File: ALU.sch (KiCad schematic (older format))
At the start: 30 parts, among them U42 74LS245, U43 74LS00, U44 74LS86, U45 74LS86, U46 74LS86, U47 74LS00, U48 74LS86, U49 74HC02, U50 74LS00, U51 74LS00, U52 74LS283, U53 74LS85, U54 74LS283, U55 74LS245, U56 74LS85, U57 74LS245, U58 74LS283, U59 74LS85, U60 74LS173, U61 74LS283, U62 74LS245, U63 74LS85

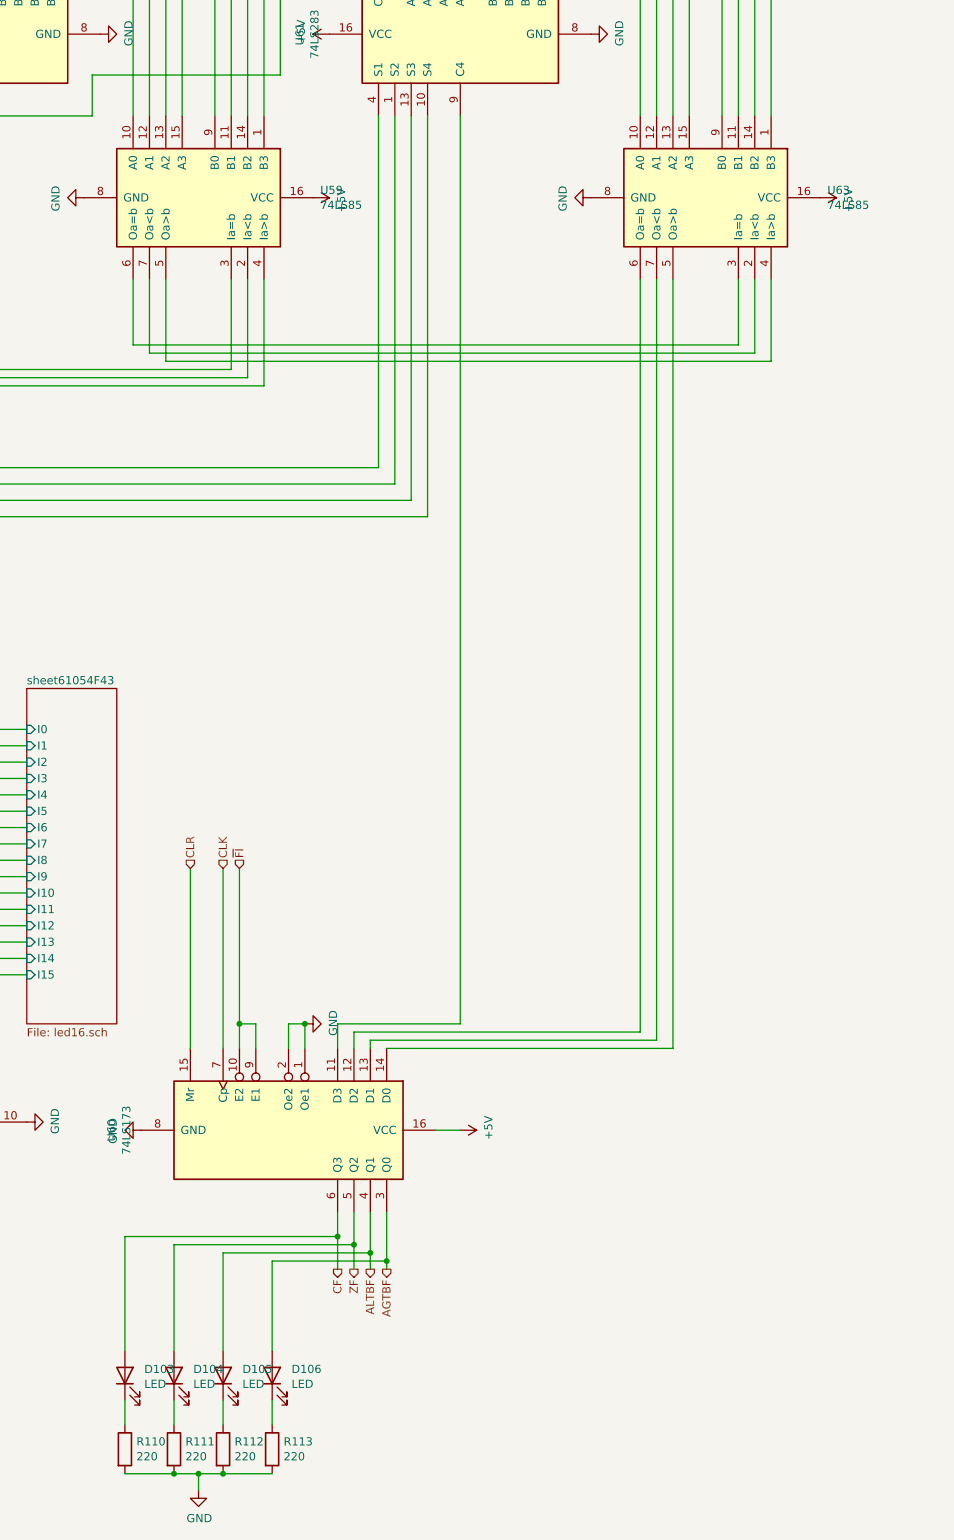
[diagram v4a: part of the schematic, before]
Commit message: added 3-8 decoders to cu
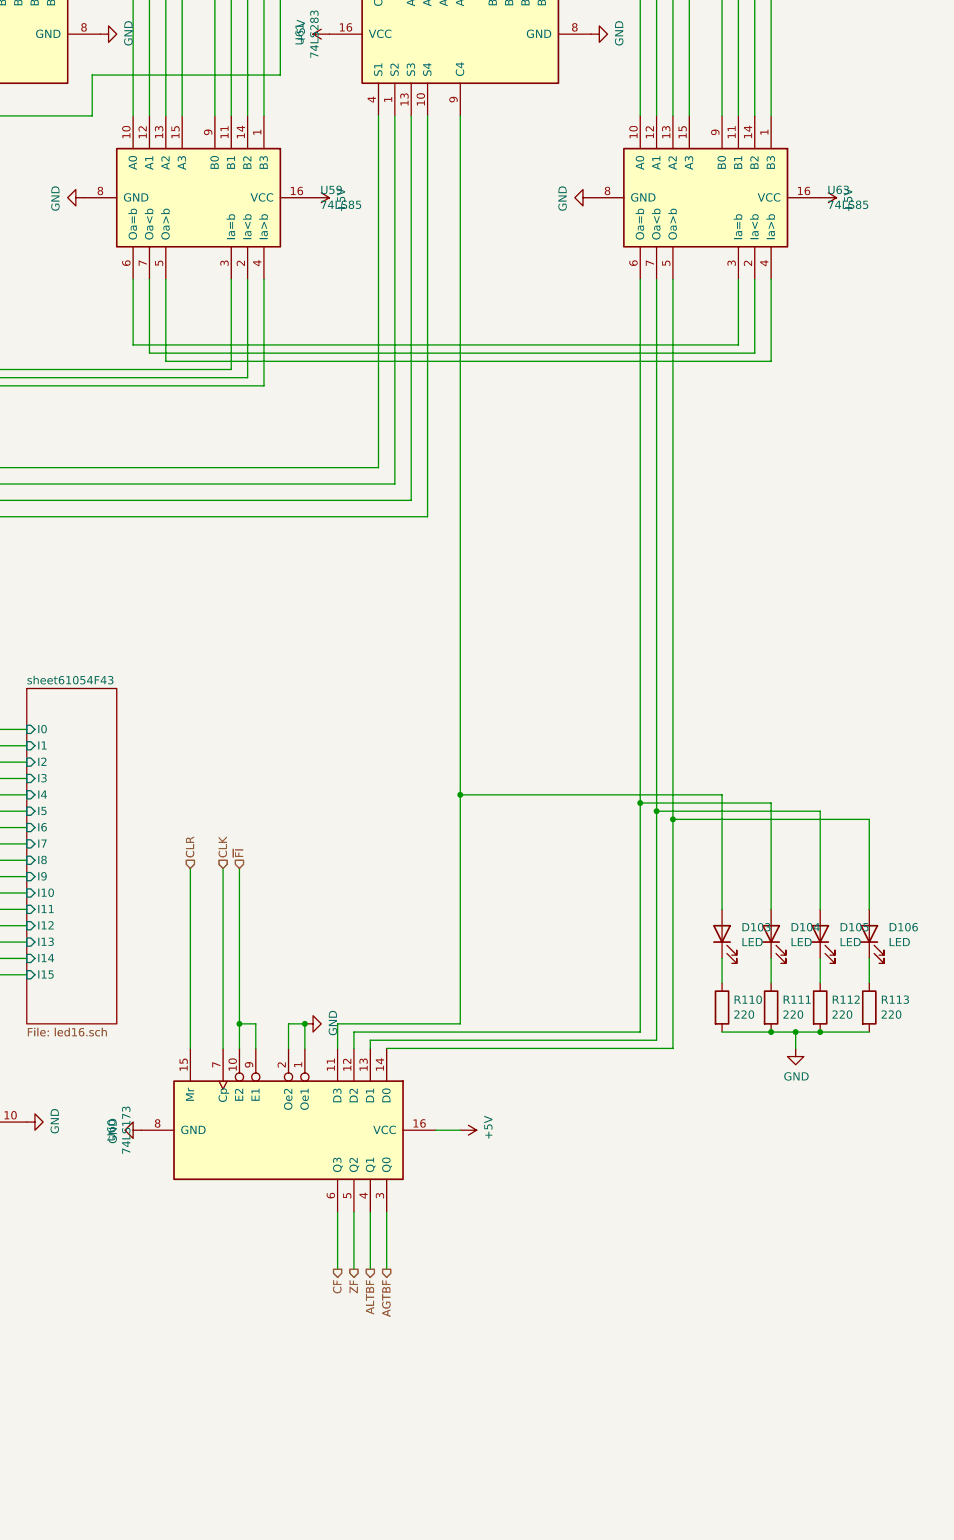
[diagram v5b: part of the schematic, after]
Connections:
- net AGTBF: no longer D106.2 (A)
- net ALTBF: no longer D105.2 (A)
- net CF: no longer D103.2 (A)
- net ZF: no longer D104.2 (A)
- net at U60.11 (D3), U61.9 (C4): now also D103.2 (A)
- net at U60.12 (D2), U63.6 (Oa=b): now also D104.2 (A)
- net at U60.13 (D1), U63.7 (Oa<b): now also D105.2 (A)
- net at U60.14 (D0), U63.5 (Oa>b): now also D106.2 (A)
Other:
- moved on the sheet: D103, D104, D105, D106, R110, R111, R112, R113
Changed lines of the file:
@@
 Text HLabel 17700 18700 3    50   Output ~ 0
 ZF
-Wire Wire Line
-	17700 18350 17700 18550
 Text HLabel 17600 18700 3    50   Output ~ 0
 CF
 Wire Wire Line
 	17000 17200 17000 16250
-Wire Wire Line
-	17600 18350 17600 18500
 Text HLabel 16700 16250 1    50   Input ~ 0
 CLR
@@
 	17900 17350 19650 17350
 Wire Wire Line
-	19650 17350 19650 12650
-Wire Wire Line
-	19550 12650 19550 17300
+	19550 12650 19550 15900
 Wire Wire Line
 	19550 17300 17800 17300
@@
 	17700 17250 19450 17250
 Wire Wire Line
-	19450 17250 19450 12650
-Wire Wire Line
-	18350 11650 18350 17200
+	19450 17250 19450 15850
+Wire Wire Line
+	18350 11650 18350 15800
 Wire Wire Line
 	18350 17200 17600 17200
@@
 Text HLabel 17800 18700 3    50   Output ~ 0
 ALTBF
-Wire Wire Line
-	17800 18350 17800 18600
 Text HLabel 17900 18700 3    50   Output ~ 0
 AGTBF
 Wire Wire Line
-	17900 18350 17900 18650
-Wire Wire Line
 	15700 15400 12450 15400
 Wire Wire Line
@@
 L Device:LED D?
 U 1 1 6367F2BC
-P 16600 19350
+P 20250 16650
 AR Path="/5F926C74/6367F2BC" Ref="D?"  Part="1"
 AR Path="/61968B9B/60C9B37A/6367F2BC" Ref="D?"  Part="1"
@@
 AR Path="/5FD099BF/625B6FDA/6367F2BC" Ref="D?"  Part="1"
 AR Path="/5F5F4A69/6367F2BC" Ref="D104"  Part="1"
-F 0 "D104" V 16639 19232 50  0000 R CNN
-F 1 "LED" V 16548 19232 50  0000 R CNN
-F 2 "LED_THT:LED_D3.0mm" H 16600 19350 50  0001 C CNN
-F 3 "" H 16600 19350 50  0001 C CNN
-	1    16600 19350
+F 0 "D104" V 20289 16532 50  0000 R CNN
+F 1 "LED" V 20198 16532 50  0000 R CNN
+F 2 "LED_THT:LED_D3.0mm" H 20250 16650 50  0001 C CNN
+F 3 "" H 20250 16650 50  0001 C CNN
+	1    20250 16650
 	0    -1   -1   0
 $EndComp
@@
 L Device:LED D?
 U 1 1 6367F2C2
-P 16900 19350
+P 20550 16650
 AR Path="/5F926C74/6367F2C2" Ref="D?"  Part="1"
 AR Path="/61968B9B/60C9B37A/6367F2C2" Ref="D?"  Part="1"
@@
 AR Path="/5FD099BF/625B6FDA/6367F2C2" Ref="D?"  Part="1"
 AR Path="/5F5F4A69/6367F2C2" Ref="D105"  Part="1"
-F 0 "D105" V 16939 19232 50  0000 R CNN
-F 1 "LED" V 16848 19232 50  0000 R CNN
-F 2 "LED_THT:LED_D3.0mm" H 16900 19350 50  0001 C CNN
-F 3 "" H 16900 19350 50  0001 C CNN
-	1    16900 19350
+F 0 "D105" V 20589 16532 50  0000 R CNN
+F 1 "LED" V 20498 16532 50  0000 R CNN
+F 2 "LED_THT:LED_D3.0mm" H 20550 16650 50  0001 C CNN
+F 3 "" H 20550 16650 50  0001 C CNN
+	1    20550 16650
 	0    -1   -1   0
 $EndComp
@@
 L Device:LED D?
 U 1 1 6367F2C8
-P 17200 19350
+P 20850 16650
 AR Path="/5F926C74/6367F2C8" Ref="D?"  Part="1"
 AR Path="/61968B9B/60C9B37A/6367F2C8" Ref="D?"  Part="1"
@@
 AR Path="/5FD099BF/625B6FDA/6367F2C8" Ref="D?"  Part="1"
 AR Path="/5F5F4A69/6367F2C8" Ref="D106"  Part="1"
-F 0 "D106" V 17239 19232 50  0000 R CNN
-F 1 "LED" V 17148 19232 50  0000 R CNN
-F 2 "LED_THT:LED_D3.0mm" H 17200 19350 50  0001 C CNN
-F 3 "" H 17200 19350 50  0001 C CNN
-	1    17200 19350
+F 0 "D106" V 20889 16532 50  0000 R CNN
+F 1 "LED" V 20798 16532 50  0000 R CNN
+F 2 "LED_THT:LED_D3.0mm" H 20850 16650 50  0001 C CNN
+F 3 "" H 20850 16650 50  0001 C CNN
+	1    20850 16650
 	0    -1   -1   0
 $EndComp
 Wire Wire Line
-	16600 19500 16600 19650
-Wire Wire Line
-	16900 19500 16900 19650
-Wire Wire Line
-	17200 19500 17200 19650
+	20250 16800 20250 16950
+Wire Wire Line
+	20550 16800 20550 16950
+Wire Wire Line
+	20850 16800 20850 16950
 $Comp
 L Device:R R?
 U 1 1 6367F2D7
-P 16600 19800
+P 20250 17100
 AR Path="/5F926C74/6367F2D7" Ref="R?"  Part="1"
 AR Path="/61968B9B/60C9B37A/6367F2D7" Ref="R?"  Part="1"
@@
 AR Path="/5FD099BF/625B6FDA/6367F2D7" Ref="R?"  Part="1"
 AR Path="/5F5F4A69/6367F2D7" Ref="R111"  Part="1"
-F 0 "R111" H 16670 19846 50  0000 L CNN
-F 1 "220" H 16670 19755 50  0000 L CNN
-F 2 "Resistor_THT:R_Axial_DIN0204_L3.6mm_D1.6mm_P7.62mm_Horizontal" V 16530 19800 50  0001 C CNN
-F 3 "" H 16600 19800 50  0001 C CNN
-	1    16600 19800
+F 0 "R111" H 20320 17146 50  0000 L CNN
+F 1 "220" H 20320 17055 50  0000 L CNN
+F 2 "Resistor_THT:R_Axial_DIN0204_L3.6mm_D1.6mm_P7.62mm_Horizontal" V 20180 17100 50  0001 C CNN
+F 3 "" H 20250 17100 50  0001 C CNN
+	1    20250 17100
 	1    0    0    -1
 $EndComp
@@
 L Device:R R?
 U 1 1 6367F2DD
-P 16900 19800
+P 20550 17100
 AR Path="/5F926C74/6367F2DD" Ref="R?"  Part="1"
 AR Path="/61968B9B/60C9B37A/6367F2DD" Ref="R?"  Part="1"
@@
 AR Path="/5FD099BF/625B6FDA/6367F2DD" Ref="R?"  Part="1"
 AR Path="/5F5F4A69/6367F2DD" Ref="R112"  Part="1"
-F 0 "R112" H 16970 19846 50  0000 L CNN
-F 1 "220" H 16970 19755 50  0000 L CNN
-F 2 "Resistor_THT:R_Axial_DIN0204_L3.6mm_D1.6mm_P7.62mm_Horizontal" V 16830 19800 50  0001 C CNN
-F 3 "" H 16900 19800 50  0001 C CNN
-	1    16900 19800
+F 0 "R112" H 20620 17146 50  0000 L CNN
+F 1 "220" H 20620 17055 50  0000 L CNN
+F 2 "Resistor_THT:R_Axial_DIN0204_L3.6mm_D1.6mm_P7.62mm_Horizontal" V 20480 17100 50  0001 C CNN
+F 3 "" H 20550 17100 50  0001 C CNN
+	1    20550 17100
 	1    0    0    -1
 $EndComp
@@
 L Device:R R?
 U 1 1 6367F2E3
-P 17200 19800
+P 20850 17100
 AR Path="/5F926C74/6367F2E3" Ref="R?"  Part="1"
 AR Path="/61968B9B/60C9B37A/6367F2E3" Ref="R?"  Part="1"
@@
 AR Path="/5FD099BF/625B6FDA/6367F2E3" Ref="R?"  Part="1"
 AR Path="/5F5F4A69/6367F2E3" Ref="R113"  Part="1"
-F 0 "R113" H 17270 19846 50  0000 L CNN
-F 1 "220" H 17270 19755 50  0000 L CNN
-F 2 "Resistor_THT:R_Axial_DIN0204_L3.6mm_D1.6mm_P7.62mm_Horizontal" V 17130 19800 50  0001 C CNN
-F 3 "" H 17200 19800 50  0001 C CNN
-	1    17200 19800
+F 0 "R113" H 20920 17146 50  0000 L CNN
+F 1 "220" H 20920 17055 50  0000 L CNN
+F 2 "Resistor_THT:R_Axial_DIN0204_L3.6mm_D1.6mm_P7.62mm_Horizontal" V 20780 17100 50  0001 C CNN
+F 3 "" H 20850 17100 50  0001 C CNN
+	1    20850 17100
 	1    0    0    -1
 $EndComp
 Wire Wire Line
-	16300 19950 16600 19950
-Connection ~ 16600 19950
-Wire Wire Line
-	16600 19950 16750 19950
-Connection ~ 16900 19950
-Wire Wire Line
-	16900 19950 17200 19950
+	19950 17250 20250 17250
+Connection ~ 20250 17250
+Wire Wire Line
+	20250 17250 20400 17250
+Connection ~ 20550 17250
+Wire Wire Line
+	20550 17250 20850 17250
 $Comp
 L Device:LED D?
 U 1 1 636C3FB6
-P 16300 19350
+P 19950 16650
 AR Path="/5F926C74/636C3FB6" Ref="D?"  Part="1"
 AR Path="/61968B9B/60C9B37A/636C3FB6" Ref="D?"  Part="1"
@@
 AR Path="/5FD099BF/625B6FDA/636C3FB6" Ref="D?"  Part="1"
 AR Path="/5F5F4A69/636C3FB6" Ref="D103"  Part="1"
-F 0 "D103" V 16339 19232 50  0000 R CNN
-F 1 "LED" V 16248 19232 50  0000 R CNN
-F 2 "LED_THT:LED_D3.0mm" H 16300 19350 50  0001 C CNN
-F 3 "" H 16300 19350 50  0001 C CNN
-	1    16300 19350
+F 0 "D103" V 19989 16532 50  0000 R CNN
+F 1 "LED" V 19898 16532 50  0000 R CNN
+F 2 "LED_THT:LED_D3.0mm" H 19950 16650 50  0001 C CNN
+F 3 "" H 19950 16650 50  0001 C CNN
+	1    19950 16650
 	0    -1   -1   0
 $EndComp
 Wire Wire Line
-	16300 19500 16300 19650
+	19950 16800 19950 16950
 $Comp
 L Device:R R?
 U 1 1 636C3FBF
-P 16300 19800
+P 19950 17100
 AR Path="/5F926C74/636C3FBF" Ref="R?"  Part="1"
 AR Path="/61968B9B/60C9B37A/636C3FBF" Ref="R?"  Part="1"
@@
 AR Path="/5FD099BF/625B6FDA/636C3FBF" Ref="R?"  Part="1"
 AR Path="/5F5F4A69/636C3FBF" Ref="R110"  Part="1"
-F 0 "R110" H 16370 19846 50  0000 L CNN
-F 1 "220" H 16370 19755 50  0000 L CNN
-F 2 "Resistor_THT:R_Axial_DIN0204_L3.6mm_D1.6mm_P7.62mm_Horizontal" V 16230 19800 50  0001 C CNN
-F 3 "" H 16300 19800 50  0001 C CNN
-	1    16300 19800
+F 0 "R110" H 20020 17146 50  0000 L CNN
+F 1 "220" H 20020 17055 50  0000 L CNN
+F 2 "Resistor_THT:R_Axial_DIN0204_L3.6mm_D1.6mm_P7.62mm_Horizontal" V 19880 17100 50  0001 C CNN
+F 3 "" H 19950 17100 50  0001 C CNN
+	1    19950 17100
 	1    0    0    -1
 $EndComp
 Wire Wire Line
-	17200 18650 17900 18650
-Wire Wire Line
-	17200 18650 17200 19200
-Connection ~ 17900 18650
-Wire Wire Line
-	17900 18650 17900 18700
-Wire Wire Line
-	16900 18600 17800 18600
-Wire Wire Line
-	16900 18600 16900 19200
-Connection ~ 17800 18600
-Wire Wire Line
-	17800 18600 17800 18700
-Wire Wire Line
-	17700 18550 16600 18550
-Wire Wire Line
-	16600 18550 16600 19200
-Connection ~ 17700 18550
-Wire Wire Line
-	17700 18550 17700 18700
-Wire Wire Line
-	16300 18500 17600 18500
-Wire Wire Line
-	16300 18500 16300 19200
-Connection ~ 17600 18500
-Wire Wire Line
-	17600 18500 17600 18700
+	20850 15950 20850 16500
+Wire Wire Line
+	20550 15900 20550 16500
+Wire Wire Line
+	20250 15850 20250 16500
+Wire Wire Line
+	19950 15800 19950 16500
 $Comp
 L 16bitCpu-rescue:GND-power #PWR?
 U 1 1 6385D433
-P 16750 20050
+P 20400 17350
 AR Path="/6385D433" Ref="#PWR?"  Part="1"
 AR Path="/5F5F4A69/6385D433" Ref="#PWR0180"  Part="1"
-F 0 "#PWR0180" H 16750 19800 50  0001 C CNN
-F 1 "GND" H 16755 19877 50  0000 C CNN
-F 2 "" H 16750 20050 50  0001 C CNN
-F 3 "" H 16750 20050 50  0001 C CNN
-	1    16750 20050
+F 0 "#PWR0180" H 20400 17100 50  0001 C CNN
+F 1 "GND" H 20405 17177 50  0000 C CNN
+F 2 "" H 20400 17350 50  0001 C CNN
+F 3 "" H 20400 17350 50  0001 C CNN
+	1    20400 17350
 	1    0    0    -1
 $EndComp
 Wire Wire Line
-	16750 19950 16750 20050
-Connection ~ 16750 19950
-Wire Wire Line
-	16750 19950 16900 19950
+	20400 17250 20400 17350
+Connection ~ 20400 17250
+Wire Wire Line
+	20400 17250 20550 17250
 Wire Wire Line
 	8250 2800 8250 6050
@@
 Wire Wire Line
 	3650 2200 3650 6700
+Wire Wire Line
+	17700 18350 17700 18700
+Wire Wire Line
+	17600 18350 17600 18700
+Wire Wire Line
+	17800 18350 17800 18700
+Wire Wire Line
+	17900 18350 17900 18700
+Wire Wire Line
+	20850 15950 19650 15950
+Wire Wire Line
+	19650 12650 19650 15950
+Connection ~ 19650 15950
+Wire Wire Line
+	19650 15950 19650 17350
+Wire Wire Line
+	20550 15900 19550 15900
+Connection ~ 19550 15900
+Wire Wire Line
+	19550 15900 19550 17300
+Wire Wire Line
+	20250 15850 19450 15850
+Connection ~ 19450 15850
+Wire Wire Line
+	19450 15850 19450 12650
+Wire Wire Line
+	19950 15800 18350 15800
+Connection ~ 18350 15800
+Wire Wire Line
+	18350 15800 18350 17200
 $EndSCHEMATC

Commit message: using new RAM and ROM,15bits baby
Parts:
- renumbered U42 to U45, U43 to U46, U44 to U47, U45 to U48, U46 to U49, U47 to U50, U48 to U51, U49 to U52, U50 to U53, U51 to U54, U52 to U55, U53 to U56, U54 to U57, U55 to U58, U56 to U59, U57 to U60, U58 to U61, U59 to U62, U60 to U63, U61 to U64, U62 to U65, U63 to U66

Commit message: using new ROM in CU and more jumps
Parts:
- renumbered U45 to U44, U46 to U45, U47 to U46, U48 to U47, U49 to U48, U50 to U49, U51 to U50, U52 to U51, U53 to U52, U54 to U53, U55 to U54, U56 to U55, U57 to U56, U58 to U57, U59 to U58, U60 to U59, U61 to U60, U62 to U61, U63 to U62, U64 to U63, U65 to U64, U66 to U65

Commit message: fixed almost all errors
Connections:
- net GND: now also U55.8 (GND)
- net SU: now also U54.7 (C0)
- net at U48.11, U53.13, U56.11 (B4)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: no longer U45.2, U47.3, U60.6 (B1), U61.9 (B0)
- net at U55.5 (Oa>b): now also U58.3 (Ia=b); no longer U58.5 (Oa>b)
- net at U55.6 (Oa=b): now also U58.4 (Ia>b); no longer U58.6 (Oa=b)
- net at U55.7 (Oa<b): now also U58.2 (Ia<b); no longer U58.7 (Oa<b)
- net at U61.2 (Ia<b): now also U58.7 (Oa<b); no longer U58.2 (Ia<b)
- net at U61.3 (Ia=b): now also U58.6 (Oa=b); no longer U58.3 (Ia=b)
- net at U61.4 (Ia>b): now also U58.5 (Oa>b); no longer U58.4 (Ia>b)
- new net: U45.2, U47.3, U60.6 (B1), U61.9 (B0)
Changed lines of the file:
@@
 	18350 9450 9650 9450
-Wire Wire Line
-	12700 7750 12750 7750
 Wire Wire Line
 	12750 7750 12750 9400
@@
 	10750 12650 10750 13350
 Wire Wire Line
-	10750 13350 13450 13350
-Wire Wire Line
-	13450 13350 13450 12650
-Wire Wire Line
-	10850 13300 13350 13300
-Wire Wire Line
-	13350 13300 13350 12650
-Wire Wire Line
 	10850 12650 10850 13300
 Wire Wire Line
-	13250 12650 13250 13250
-Wire Wire Line
-	13250 13250 10950 13250
-Wire Wire Line
 	10950 13250 10950 12650
-Wire Wire Line
-	14050 12650 14050 13300
-Wire Wire Line
-	14050 13300 17150 13300
-Wire Wire Line
-	17150 13300 17150 12650
-Wire Wire Line
-	17050 12650 17050 13250
-Wire Wire Line
-	17050 13250 13950 13250
-Wire Wire Line
-	13950 13250 13950 12650
-Wire Wire Line
-	13850 12650 13850 13200
-Wire Wire Line
-	16950 13200 16950 12650
-Wire Wire Line
-	13850 13200 16950 13200
 Wire Wire Line
 	16550 12650 16550 13150
@@
 	12700 4750 12700 6200
 Connection ~ 12700 7800
-Connection ~ 12700 7750
-Wire Wire Line
-	12700 7750 12700 7800
 $Comp
 L 74xx:74LS00 U45
@@
 Wire Wire Line
 	6600 6200 12700 6200
-Connection ~ 12700 6200
-Wire Wire Line
-	12700 6200 12700 7750
 Wire Wire Line
 	6050 6450 12950 6450
@@
 Wire Wire Line
 	18350 15800 18350 17200
+Wire Wire Line
+	14050 13250 14050 12650
+Wire Wire Line
+	10950 13250 14050 13250
+Wire Wire Line
+	13950 13300 13950 12650
+Wire Wire Line
+	10850 13300 13950 13300
+Wire Wire Line
+	13850 13350 13850 12650
+Wire Wire Line
+	10750 13350 13850 13350
+Wire Wire Line
+	13450 13500 17150 13500
+Wire Wire Line
+	17150 12650 17150 13500
+Wire Wire Line
+	17050 12650 17050 13450
+Wire Wire Line
+	13350 12650 13350 13450
+Wire Wire Line
+	13450 12650 13450 13500
+Wire Wire Line
+	13350 13450 17050 13450
+Wire Wire Line
+	13250 13400 16950 13400
+Wire Wire Line
+	16950 12650 16950 13400
+Wire Wire Line
+	12700 7750 12750 7750
+Connection ~ 12700 6200
+Wire Wire Line
+	12700 6200 12700 7750
+Wire Wire Line
+	13250 12650 13250 13400
+$Comp
+L 16bitCpu-rescue:GND-power #PWR?
+U 1 1 63517C37
+P 11250 12150
+AR Path="/63517C37" Ref="#PWR?"  Part="1"
+AR Path="/5F5F4A69/63517C37" Ref="#PWR0261"  Part="1"
+F 0 "#PWR0261" H 11250 11900 50  0001 C CNN
+F 1 "GND" H 11255 11977 50  0000 C CNN
+F 2 "" H 11250 12150 50  0001 C CNN
+F 3 "" H 11250 12150 50  0001 C CNN
+	1    11250 12150
+	0    -1   -1   0
+$EndComp
+Wire Wire Line
+	10450 4900 7050 4900
+Wire Wire Line
+	7050 4900 7050 10650
+Wire Wire Line
+	7050 10650 8600 10650
+Connection ~ 10450 4900
 $EndSCHEMATC
